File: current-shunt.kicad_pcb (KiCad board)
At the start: 4 copper layers, 130 x 50 mm, 183 parts, among them J1 Screw_Terminal_01x03, J2 Screw_Terminal_01x03, J3 Screw_Terminal_01x03, J4 Conn_01x02, J5 Conn_01x04, J6 Conn_01x04, U1 ADS1015IDGS, U2 INA219AxD, U3 INA219AxD, U4 INA219AxD, U5 MCP9804_MSOP, U6 M24C02-WMN, U7 TSR_1-2450, U8 ISO1541, U9 SRV05-4

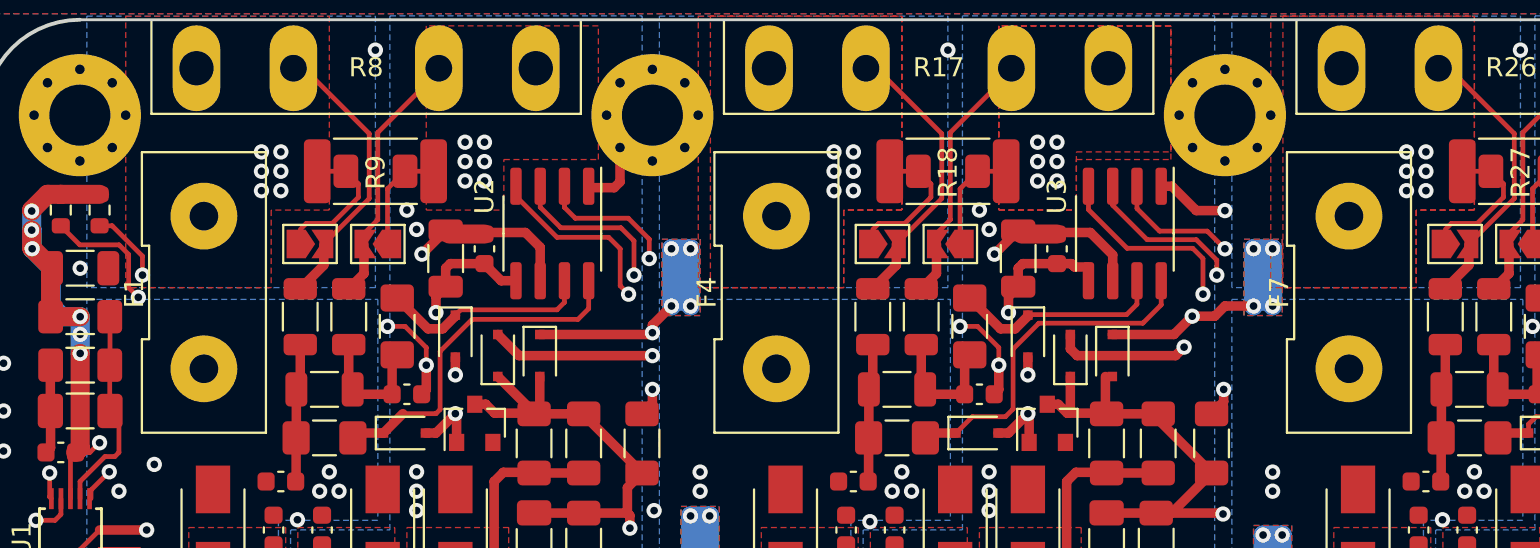
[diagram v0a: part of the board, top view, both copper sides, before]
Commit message: Update iMaXX H7810 footprint
Finally found a better datasheet with more measurements.
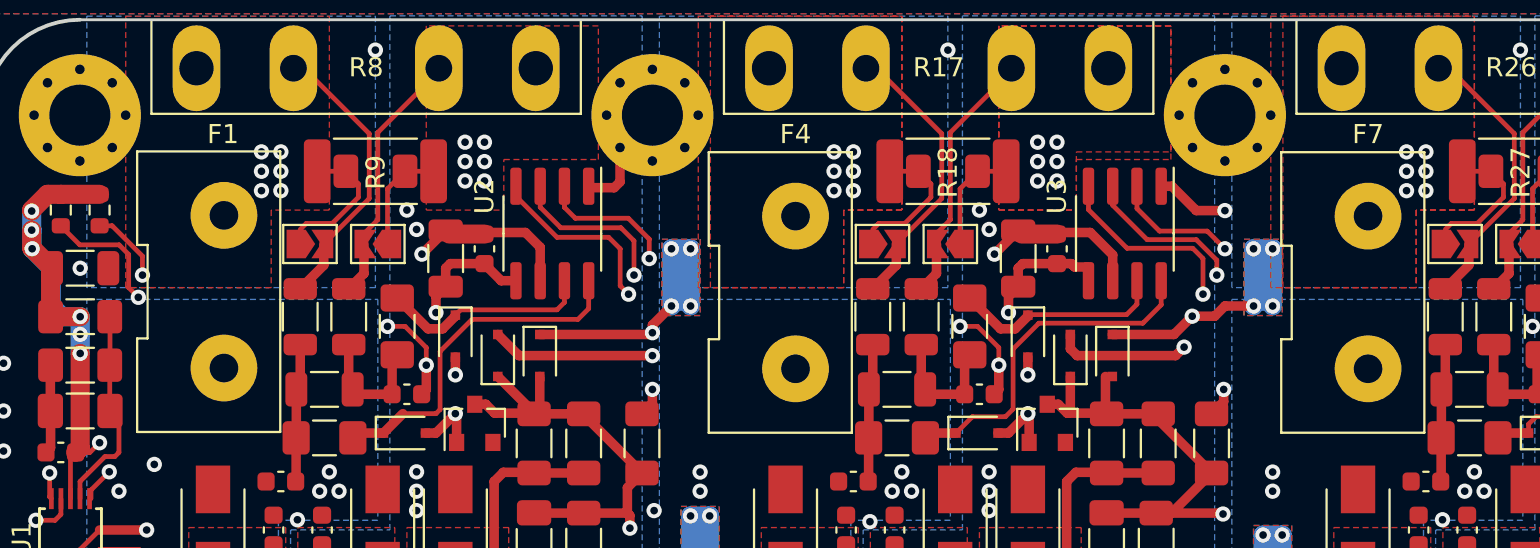
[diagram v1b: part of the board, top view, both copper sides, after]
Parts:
- moved F1 1.05 mm to (62.5, 34.2)
- moved F4 1.00 mm to (92.5, 34.3)
- moved F7 1.00 mm to (122.5, 34.3)
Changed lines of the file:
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@@
   )
   (footprint "Project_Footprints:iMaXX-H7810" (layer "F.Cu")
-    (at 61.5 34.29)
+    (at 62.55 34.25)
     (descr "MiniOTO Fuse Holder")
     (tags "fuse holder minioto")
@@
     (property "Sheetname" "shunt-a")
     (attr through_hole)
-    (fp_text reference "F1" (at -3.65 0 270) (layer "F.SilkS")
+    (fp_text reference "F1" (at -0.05 -8.25) (layer "F.SilkS")
       (effects (font (size 1 1) (thickness 0.15)))
     )
@@
       (effects (font (size 1 1) (thickness 0.15)))
     )
-    (fp_line (start -2.87 -2.45) (end -2.870001 2.45) (layer "F.SilkS") (width 0.12))
-    (fp_line (start -3.25 7.35) (end 3.25 7.35) (layer "F.SilkS") (width 0.12))
-    (fp_line (start 3.25 -7.35) (end -3.25 -7.35) (layer "F.SilkS") (width 0.12))
-    (fp_line (start 3.25 7.35) (end 3.25 -7.35) (layer "F.SilkS") (width 0.12))
-    (fp_line (start -3.23 -2.45) (end -2.87 -2.45) (layer "F.SilkS") (width 0.12))
-    (fp_line (start -3.25 -7.35) (end -3.25 -2.45) (layer "F.SilkS") (width 0.12))
-    (fp_line (start -3.25 2.45) (end -3.25 7.35) (layer "F.SilkS") (width 0.12))
-    (fp_line (start -2.89 2.45) (end -3.25 2.45) (layer "F.SilkS") (width 0.12))
-    (fp_line (start -3 -7.1) (end 3 -7.1) (layer "F.CrtYd") (width 0.05))
-    (fp_line (start 3 -7.1) (end 3 7.1) (layer "F.CrtYd") (width 0.05))
-    (fp_line (start 3 7.1) (end -3 7.1) (layer "F.CrtYd") (width 0.05))
-    (fp_line (start -3 7.1) (end -3 -7.1) (layer "F.CrtYd") (width 0.05))
+    (fp_line (start -3.999999 -2.45) (end -4 2.45) (layer "F.SilkS") (width 0.12))
+    (fp_line (start -4.55 -2.45) (end -3.999999 -2.45) (layer "F.SilkS") (width 0.12))
+    (fp_line (start -4.019999 2.45) (end -4.55 2.45) (layer "F.SilkS") (width 0.12))
+    (fp_line (start -4.55 -7.35) (end -4.55 -2.45) (layer "F.SilkS") (width 0.12))
+    (fp_line (start 2.95 -7.35) (end -4.55 -7.35) (layer "F.SilkS") (width 0.12))
+    (fp_line (start -4.55 2.45) (end -4.55 7.35) (layer "F.SilkS") (width 0.12))
+    (fp_line (start 2.95 7.35) (end 2.95 -7.35) (layer "F.SilkS") (width 0.12))
+    (fp_line (start -4.55 7.35) (end 2.95 7.35) (layer "F.SilkS") (width 0.12))
+    (fp_rect (start -4.3 -7.1) (end 2.7 7.1) (layer "F.CrtYd") (width 0.05) (fill none))
     (pad "1" thru_hole circle (at 0 4) (size 3.5 3.5) (drill 1.5) (layers *.Cu *.Mask)
       (net 1 "/shunt-a/IN+") (pintype "passive"))
@@
   )
   (footprint "Project_Footprints:iMaXX-H7810" (layer "F.Cu")
-    (at 121.5 34.29)
+    (at 122.5 34.29)
     (descr "MiniOTO Fuse Holder")
     (tags "fuse holder minioto")
@@
     (property "Sheetname" "shunt-c")
     (attr through_hole)
-    (fp_text reference "F7" (at -3.65 0 270) (layer "F.SilkS")
+    (fp_text reference "F7" (at 0 -8.29) (layer "F.SilkS")
       (effects (font (size 1 1) (thickness 0.15)))
     )
@@
       (effects (font (size 1 1) (thickness 0.15)))
     )
-    (fp_line (start -2.89 2.45) (end -3.25 2.45) (layer "F.SilkS") (width 0.12))
-    (fp_line (start -2.87 -2.45) (end -2.870001 2.45) (layer "F.SilkS") (width 0.12))
-    (fp_line (start -3.25 -7.35) (end -3.25 -2.45) (layer "F.SilkS") (width 0.12))
-    (fp_line (start 3.25 -7.35) (end -3.25 -7.35) (layer "F.SilkS") (width 0.12))
-    (fp_line (start -3.23 -2.45) (end -2.87 -2.45) (layer "F.SilkS") (width 0.12))
-    (fp_line (start 3.25 7.35) (end 3.25 -7.35) (layer "F.SilkS") (width 0.12))
-    (fp_line (start -3.25 7.35) (end 3.25 7.35) (layer "F.SilkS") (width 0.12))
-    (fp_line (start -3.25 2.45) (end -3.25 7.35) (layer "F.SilkS") (width 0.12))
-    (fp_line (start -3 7.1) (end -3 -7.1) (layer "F.CrtYd") (width 0.05))
-    (fp_line (start -3 -7.1) (end 3 -7.1) (layer "F.CrtYd") (width 0.05))
-    (fp_line (start 3 7.1) (end -3 7.1) (layer "F.CrtYd") (width 0.05))
-    (fp_line (start 3 -7.1) (end 3 7.1) (layer "F.CrtYd") (width 0.05))
+    (fp_line (start -4.55 -7.35) (end -4.55 -2.45) (layer "F.SilkS") (width 0.12))
+    (fp_line (start -4.55 -2.45) (end -3.999999 -2.45) (layer "F.SilkS") (width 0.12))
+    (fp_line (start -3.999999 -2.45) (end -4 2.45) (layer "F.SilkS") (width 0.12))
+    (fp_line (start -4.019999 2.45) (end -4.55 2.45) (layer "F.SilkS") (width 0.12))
+    (fp_line (start -4.55 7.35) (end 2.95 7.35) (layer "F.SilkS") (width 0.12))
+    (fp_line (start 2.95 7.35) (end 2.95 -7.35) (layer "F.SilkS") (width 0.12))
+    (fp_line (start 2.95 -7.35) (end -4.55 -7.35) (layer "F.SilkS") (width 0.12))
+    (fp_line (start -4.55 2.45) (end -4.55 7.35) (layer "F.SilkS") (width 0.12))
+    (fp_rect (start -4.3 -7.1) (end 2.7 7.1) (layer "F.CrtYd") (width 0.05) (fill none))
     (pad "1" thru_hole circle (at 0 4) (size 3.5 3.5) (drill 1.5) (layers *.Cu *.Mask)
       (net 8 "/shunt-c/IN+") (pintype "passive"))
@@
   )
   (footprint "Project_Footprints:iMaXX-H7810" (layer "F.Cu")
-    (at 91.5 34.29)
+    (at 92.5 34.29)
     (descr "MiniOTO Fuse Holder")
     (tags "fuse holder minioto")
@@
     (property "Sheetname" "shunt-b")
     (attr through_hole)
-    (fp_text reference "F4" (at -3.65 0 270) (layer "F.SilkS")
+    (fp_text reference "F4" (at 0 -8.29) (layer "F.SilkS")
       (effects (font (size 1 1) (thickness 0.15)))
     )
@@
       (effects (font (size 1 1) (thickness 0.15)))
     )
-    (fp_line (start -2.87 -2.45) (end -2.870001 2.45) (layer "F.SilkS") (width 0.12))
-    (fp_line (start -3.23 -2.45) (end -2.87 -2.45) (layer "F.SilkS") (width 0.12))
-    (fp_line (start 3.25 -7.35) (end -3.25 -7.35) (layer "F.SilkS") (width 0.12))
-    (fp_line (start 3.25 7.35) (end 3.25 -7.35) (layer "F.SilkS") (width 0.12))
-    (fp_line (start -3.25 7.35) (end 3.25 7.35) (layer "F.SilkS") (width 0.12))
-    (fp_line (start -3.25 2.45) (end -3.25 7.35) (layer "F.SilkS") (width 0.12))
-    (fp_line (start -2.89 2.45) (end -3.25 2.45) (layer "F.SilkS") (width 0.12))
-    (fp_line (start -3.25 -7.35) (end -3.25 -2.45) (layer "F.SilkS") (width 0.12))
-    (fp_line (start 3 7.1) (end -3 7.1) (layer "F.CrtYd") (width 0.05))
-    (fp_line (start -3 7.1) (end -3 -7.1) (layer "F.CrtYd") (width 0.05))
-    (fp_line (start -3 -7.1) (end 3 -7.1) (layer "F.CrtYd") (width 0.05))
-    (fp_line (start 3 -7.1) (end 3 7.1) (layer "F.CrtYd") (width 0.05))
+    (fp_line (start -4.55 -7.35) (end -4.55 -2.45) (layer "F.SilkS") (width 0.12))
+    (fp_line (start -4.019999 2.45) (end -4.55 2.45) (layer "F.SilkS") (width 0.12))
+    (fp_line (start -3.999999 -2.45) (end -4 2.45) (layer "F.SilkS") (width 0.12))
+    (fp_line (start 2.95 7.35) (end 2.95 -7.35) (layer "F.SilkS") (width 0.12))
+    (fp_line (start -4.55 -2.45) (end -3.999999 -2.45) (layer "F.SilkS") (width 0.12))
+    (fp_line (start -4.55 7.35) (end 2.95 7.35) (layer "F.SilkS") (width 0.12))
+    (fp_line (start -4.55 2.45) (end -4.55 7.35) (layer "F.SilkS") (width 0.12))
+    (fp_line (start 2.95 -7.35) (end -4.55 -7.35) (layer "F.SilkS") (width 0.12))
+    (fp_rect (start -4.3 -7.1) (end 2.7 7.1) (layer "F.CrtYd") (width 0.05) (fill none))
     (pad "1" thru_hole circle (at 0 4) (size 3.5 3.5) (drill 1.5) (layers *.Cu *.Mask)
       (net 6 "/shunt-b/IN+") (pintype "passive"))
@@
   (gr_line (start 122.484 61.976) (end 122.484 38.1) (layer "B.Mask") (width 4))
   (gr_line (start 98.58 61.976) (end 98.58 49.276) (layer "B.Mask") (width 5))
-  (gr_line (start 62.484 61.976) (end 62.484 38.1) (layer "B.Mask") (width 4))
+  (gr_line (start 62.484 61.976) (end 62.484 38.1) (layer "B.Mask") (width 5))
   (gr_line (start 121.476 30.988) (end 121.476 22.86) (layer "B.Mask") (width 4))
   (gr_line (start 68.58 48.776) (end 78.248 48.776) (layer "B.Mask") (width 4))
   (gr_line (start 68.58 61.976) (end 68.58 49.276) (layer "B.Mask") (width 4))
-  (gr_line (start 61.476 30.988) (end 61.476 22.86) (layer "B.Mask") (width 4))
+  (gr_line (start 61.476 30.988) (end 61.476 22.86) (layer "B.Mask") (width 5))
   (gr_line (start 138.5 48.276) (end 138.5 22.86) (layer "B.Mask") (width 4))
   (gr_line (start 108.5 48.276) (end 108.5 22.86) (layer "B.Mask") (width 4))

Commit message: Update sheetname to match new use
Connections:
- net /temperature-sensor/A0 renamed /temperature-sensor-eeprom/A0
- net /temperature-sensor/A1 renamed /temperature-sensor-eeprom/A1
- net /temperature-sensor/A2 renamed /temperature-sensor-eeprom/A2
- net /temperature-sensor/ALERT renamed /temperature-sensor-eeprom/ALERT

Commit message: Add LCSC order numbers to more easily order at JLCPCB
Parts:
- C14, C16, C18, C24, C26, C28, C4, C6, C8: value 10n -> 10nF
- D15, D16, D26, D27, D4, D5: value P4SMAJ26CA -> P4SMAJ20CA
- F10, F2, F3, F5, F6, F8, F9: value Fuse_Small -> 1206L016WR
- FB1, FB2, FB3, FB4: value BLM15HB221 -> FerriteBead
